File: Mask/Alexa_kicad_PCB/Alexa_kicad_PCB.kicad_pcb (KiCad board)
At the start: 2 copper layers, 53.3 x 45.7 mm, 50 parts, among them J1 Jack-DC, J2 USB_B_Micro, J3 Conn_01x07_Male, M1 Motor_Servo, M2 Motor_Servo, M3 Motor_Servo, SW1 SW_Push, SW2 SW_Push, SW3 SW_Push, U1 TLV2372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

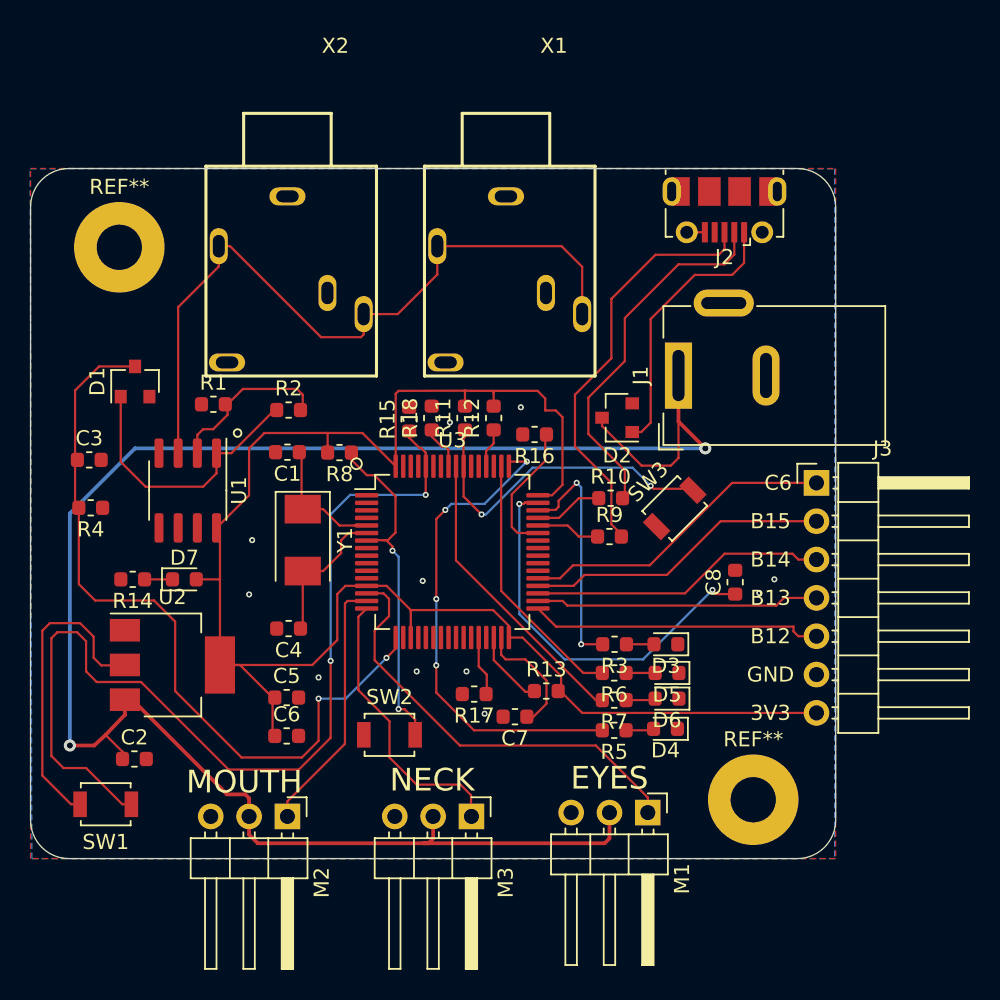
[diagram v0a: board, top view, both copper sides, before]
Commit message: cleaned up silk screen
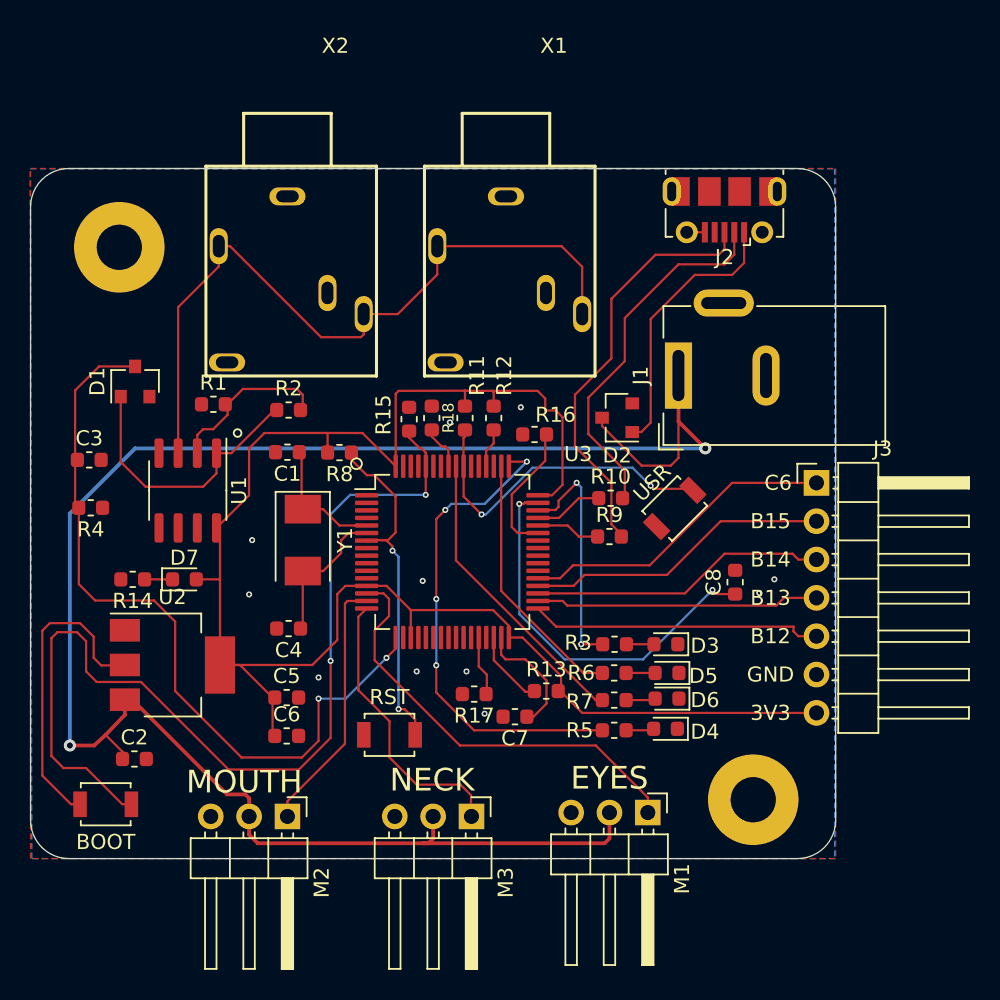
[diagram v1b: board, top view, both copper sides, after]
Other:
- board text added: "SPOOKY ALEXA V0.2"
- board text added: "WATTNOTIONS.COM/SA"
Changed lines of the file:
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@@
   (general
     (thickness 1.6)
-    (drawings 20)
+    (drawings 22)
     (tracks 383)
     (zones 0)
@@
     (tags "mounting hole 3mm")
     (attr virtual)
-    (fp_text reference REF** (at 0 -4) (layer F.SilkS)
+    (fp_text reference REF** (at 0 -4) (layer F.SilkS) hide
       (effects (font (size 1 1) (thickness 0.15)))
     )
@@
     (tags "mounting hole 3mm")
     (attr virtual)
-    (fp_text reference REF** (at 0 -4) (layer F.SilkS)
+    (fp_text reference REF** (at 0 -4) (layer F.SilkS) hide
       (effects (font (size 1 1) (thickness 0.15)))
     )
@@
     (tags "LQFP QFP")
     (attr smd)
-    (fp_text reference U3 (at 0 -7.4) (layer F.SilkS)
+    (fp_text reference U3 (at 8.34 -6.48) (layer F.SilkS)
       (effects (font (size 1 1) (thickness 0.15)))
     )
@@
     (tags diode)
     (attr smd)
-    (fp_text reference D3 (at 0 -1.43) (layer F.SilkS)
+    (fp_text reference D3 (at -2.5875 -0.1) (layer F.SilkS)
       (effects (font (size 1 1) (thickness 0.15)))
     )
@@
     (tags diode)
     (attr smd)
-    (fp_text reference D4 (at 0 -1.43) (layer F.SilkS)
+    (fp_text reference D4 (at -2.6125 -0.2) (layer F.SilkS)
       (effects (font (size 1 1) (thickness 0.15)))
     )
@@
     (tags diode)
     (attr smd)
-    (fp_text reference D5 (at 0 -1.43) (layer F.SilkS)
+    (fp_text reference D5 (at -2.4125 -0.2) (layer F.SilkS)
       (effects (font (size 1 1) (thickness 0.15)))
     )
@@
     (tags diode)
     (attr smd)
-    (fp_text reference D6 (at 0 -1.43) (layer F.SilkS)
+    (fp_text reference D6 (at -2.5125 -0.1) (layer F.SilkS)
       (effects (font (size 1 1) (thickness 0.15)))
     )
@@
     (tags resistor)
     (attr smd)
-    (fp_text reference R3 (at 0 -1.43) (layer F.SilkS)
+    (fp_text reference R3 (at 2.4125 0.1) (layer F.SilkS)
       (effects (font (size 1 1) (thickness 0.15)))
     )
@@
     (tags resistor)
     (attr smd)
-    (fp_text reference R5 (at 0 -1.43) (layer F.SilkS)
+    (fp_text reference R5 (at 2.2875 0) (layer F.SilkS)
       (effects (font (size 1 1) (thickness 0.15)))
     )
@@
     (tags resistor)
     (attr smd)
-    (fp_text reference R6 (at 0 -1.43) (layer F.SilkS)
+    (fp_text reference R6 (at 2.1875 0) (layer F.SilkS)
       (effects (font (size 1 1) (thickness 0.15)))
     )
@@
     (tags resistor)
     (attr smd)
-    (fp_text reference R7 (at 0 -1.43) (layer F.SilkS)
+    (fp_text reference R7 (at 2.2875 -0.1) (layer F.SilkS)
       (effects (font (size 1 1) (thickness 0.15)))
     )
@@
     (tags resistor)
     (attr smd)
-    (fp_text reference R11 (at 0 -1.43 90) (layer F.SilkS)
+    (fp_text reference R11 (at 2.8125 0.8 270) (layer F.SilkS)
       (effects (font (size 1 1) (thickness 0.15)))
     )
@@
     (tags resistor)
     (attr smd)
-    (fp_text reference R12 (at 0 -1.43 90) (layer F.SilkS)
+    (fp_text reference R12 (at 2.8125 0.7 90) (layer F.SilkS)
       (effects (font (size 1 1) (thickness 0.15)))
     )
@@
     (tags resistor)
     (attr smd)
-    (fp_text reference R15 (at 0 -1.43 90) (layer F.SilkS)
+    (fp_text reference R15 (at 0.2875 -1.7 90) (layer F.SilkS)
       (effects (font (size 1 1) (thickness 0.15)))
     )
@@
     (tags resistor)
     (attr smd)
-    (fp_text reference R16 (at 0 -1.43) (layer F.SilkS)
+    (fp_text reference R16 (at -1.3875 1.3) (layer F.SilkS)
       (effects (font (size 1 1) (thickness 0.15)))
     )
@@
     (tags resistor)
     (attr smd)
-    (fp_text reference R18 (at 0 -1.43 90) (layer F.SilkS)
-      (effects (font (size 1 1) (thickness 0.15)))
+    (fp_text reference R18 (at 0.0125 1.1 90) (layer F.SilkS)
+      (effects (font (size 0.75 0.75) (thickness 0.15)))
     )
     (fp_text value 100K (at 0 1.43 90) (layer F.Fab)
@@
     (tags "Tactile Switch")
     (attr smd)
-    (fp_text reference SW1 (at 0 -2.5) (layer F.SilkS)
+    (fp_text reference SW1 (at 0 -2.5) (layer F.SilkS) hide
       (effects (font (size 1 1) (thickness 0.15)))
     )
@@
     (fp_line (start 2.4 1.65) (end 2.4 -1.65) (layer F.CrtYd) (width 0.05))
     (fp_line (start -2.4 1.65) (end 2.4 1.65) (layer F.CrtYd) (width 0.05))
-    (fp_text user %R (at 0 -2.5) (layer F.Fab)
+    (fp_text user BOOT (at 0 -2.5) (layer F.SilkS)
       (effects (font (size 1 1) (thickness 0.15)))
     )
@@
     (tags "Tactile Switch")
     (attr smd)
-    (fp_text reference SW2 (at 0 -2.5) (layer F.SilkS)
+    (fp_text reference SW2 (at 0 -2.5) (layer F.SilkS) hide
       (effects (font (size 1 1) (thickness 0.15)))
     )
@@
       (effects (font (size 1 1) (thickness 0.15)))
     )
-    (fp_text user %R (at 0 -2.5) (layer F.Fab)
+    (fp_text user RST (at 0 -2.5) (layer F.SilkS)
       (effects (font (size 1 1) (thickness 0.15)))
     )
@@
     (tags "Tactile Switch")
     (attr smd)
-    (fp_text reference SW3 (at 0 -2.5 45) (layer F.SilkS)
+    (fp_text reference SW3 (at 0 -2.5 45) (layer F.SilkS) hide
       (effects (font (size 1 1) (thickness 0.15)))
     )
@@
       (effects (font (size 1 1) (thickness 0.15)))
     )
-    (fp_text user %R (at 0 -2.5 45) (layer F.Fab)
+    (fp_text user USR (at 0.141421 -2.262742 45) (layer F.SilkS)
       (effects (font (size 1 1) (thickness 0.15)))
     )
@@
     )
   )
+  (gr_text WATTNOTIONS.COM/SA (at 124.2 93.6) (layer B.SilkS)
+    (effects (font (size 1.5 1.5) (thickness 0.3)) (justify mirror))
+  )
+  (gr_text "SPOOKY ALEXA V0.2\n" (at 124.3 90.6) (layer B.SilkS)
+    (effects (font (size 1.5 1.5) (thickness 0.3) italic) (justify mirror))
+  )
   (gr_circle (center 110.236 86.106) (end 110.236 86.36) (layer F.SilkS) (width 0.12))
